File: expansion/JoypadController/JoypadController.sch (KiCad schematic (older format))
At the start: 2 parts

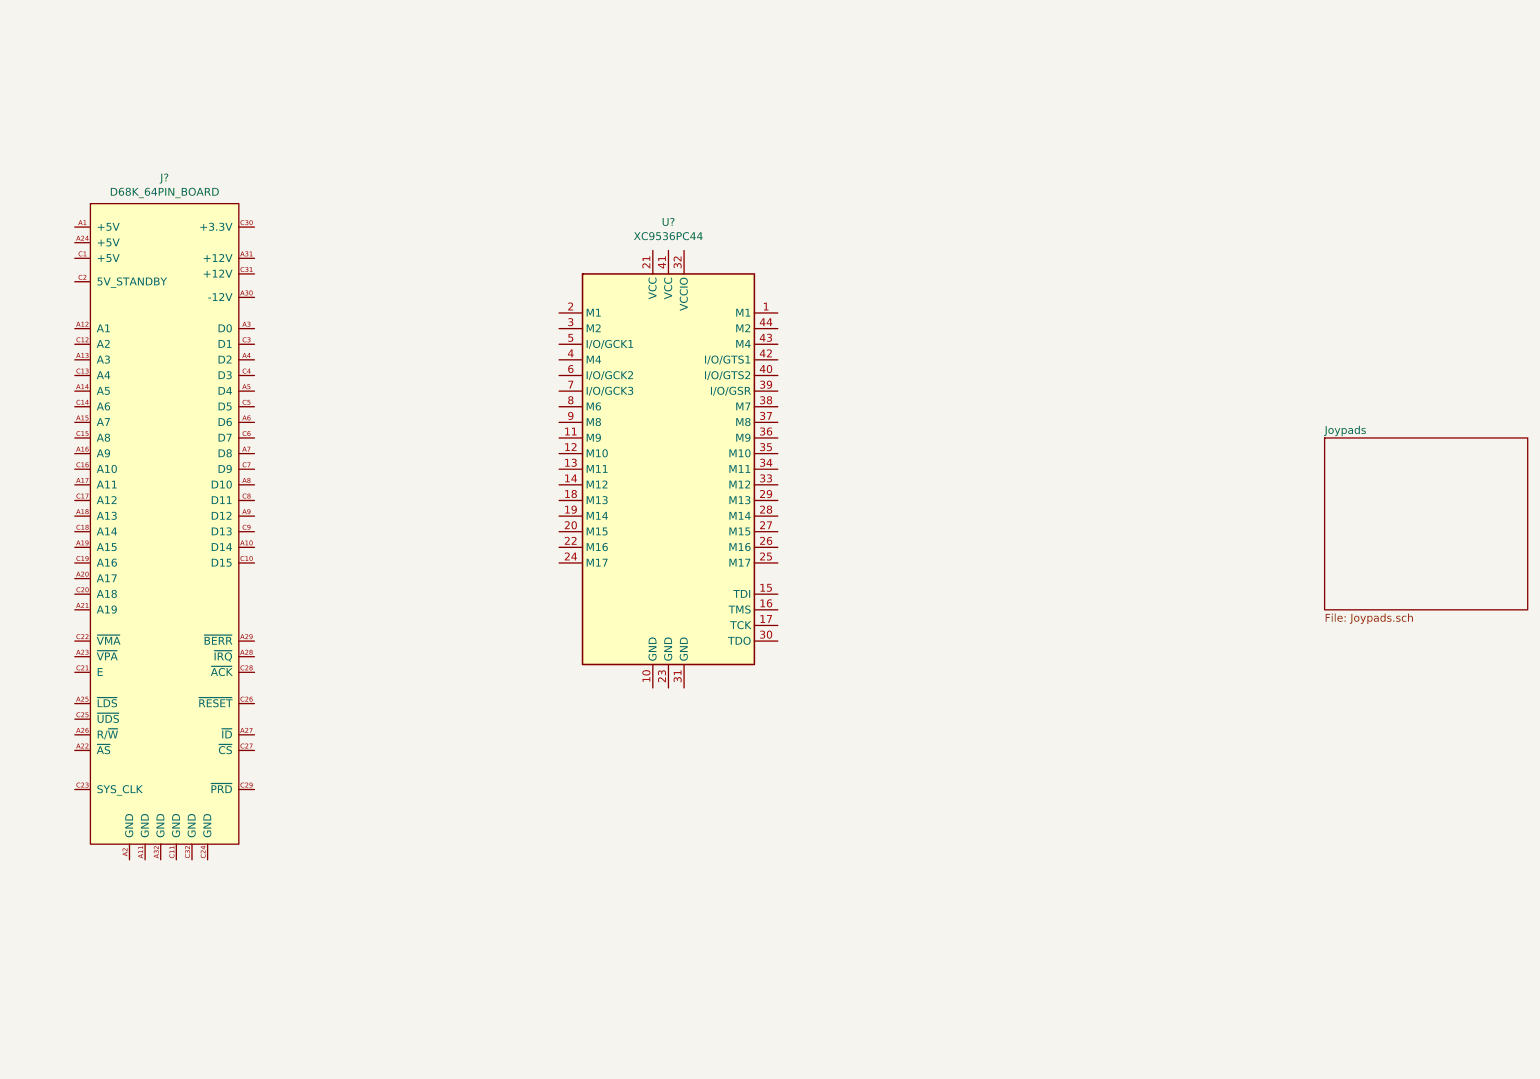
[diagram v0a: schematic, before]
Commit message: Added PCB for Joypad controller
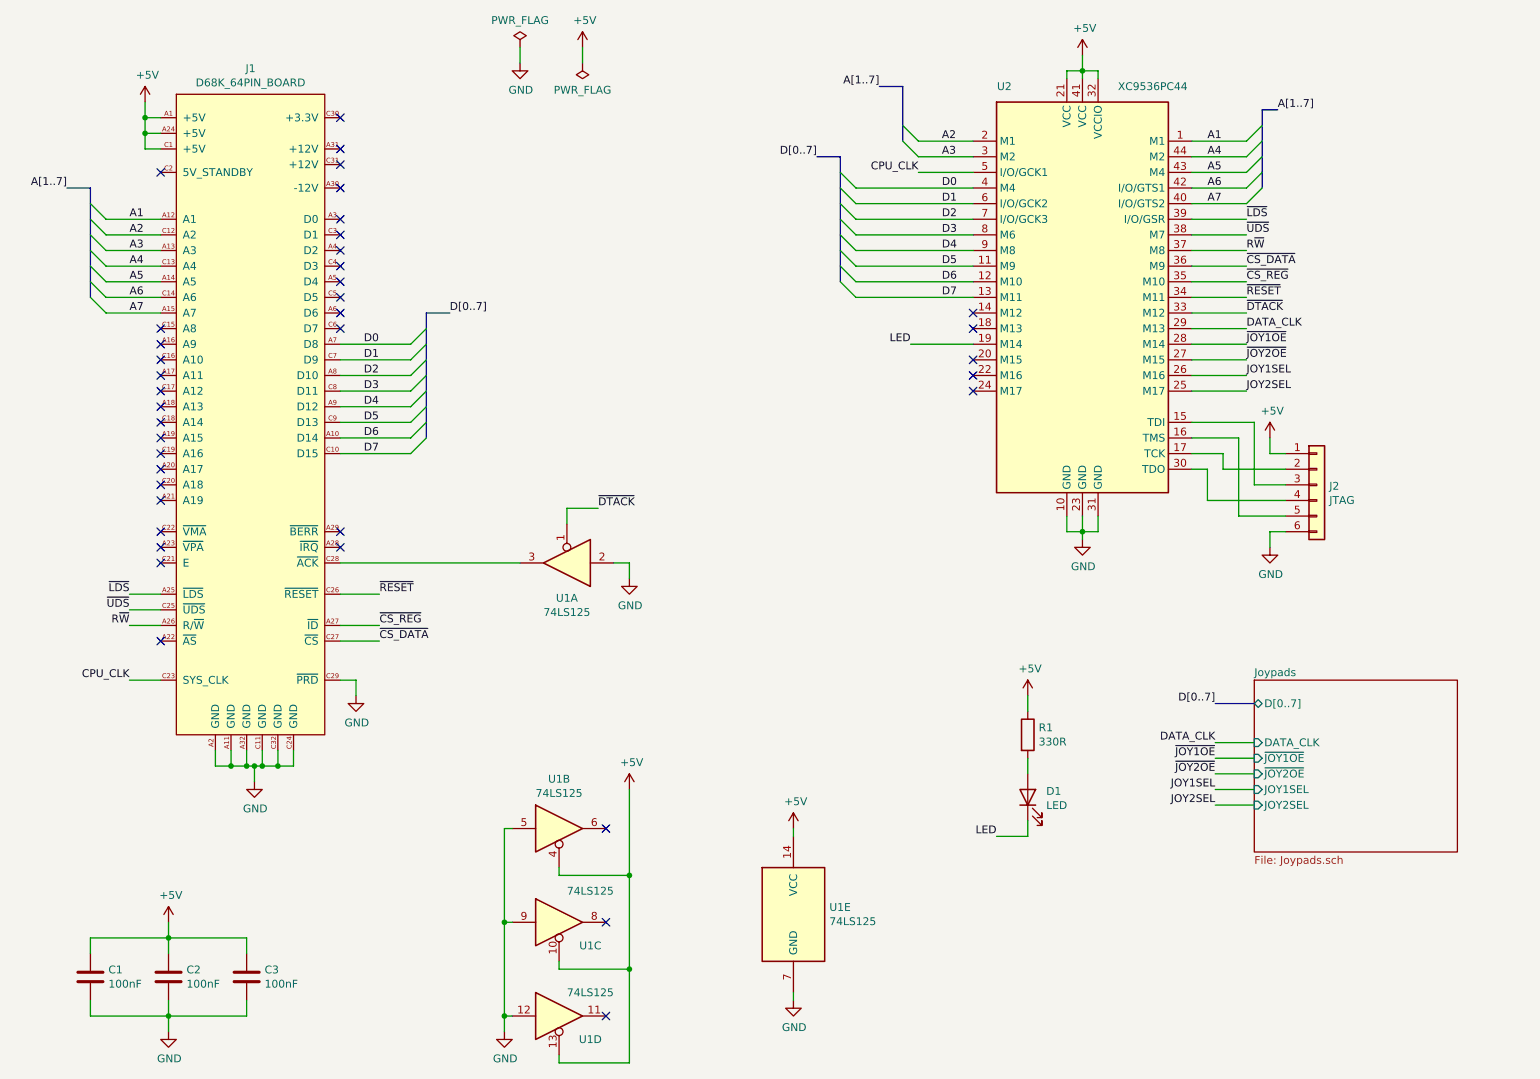
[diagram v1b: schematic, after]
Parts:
- added C1, C2, C3: 100nF, Capacitor_THT:C_Disc_D5.0mm_W2.5mm_P2.50mm, symbol Device:C
- added D1: LED, LED_THT:LED_D5.0mm, symbol Device:LED
- added J2: JTAG, Connector_PinHeader_2.54mm:PinHeader_1x06_P2.54mm_Vertical, symbol Connector_Generic:Conn_01x06
- added R1: 330R, Resistor_THT:R_Axial_DIN0207_L6.3mm_D2.5mm_P10.16mm_Horizontal, symbol Device:R
- added U1: 74LS125, Package_DIP:DIP-14_W7.62mm_Socket, symbol 74xx:74LS125
- U2: renamed from U?; footprint (none) -> Package_LCC:PLCC-44
- gave numbers to parts that had none: 1
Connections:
- net +5V: now reaches J1.A1 (+5V)
- net +5V: now also J1.A24 (+5V), J1.C1 (+5V), U2.21 (VCC), U2.32 (VCCIO), U2.41 (VCC), C1.1, C2.1, C3.1, J2.1 (Pin_1), R1.1, U1.10, U1.13, U1.14 (VCC), U1.4
- net D6: now reaches J1.A10 (D14)
- net D6: now also U2.12 (M10)
- net GND: now reaches J1.A11 (GND)
- net GND: now also J1.A2 (GND), J1.A32 (GND), J1.C11 (GND), J1.C24 (GND), J1.C29 (~PRD), J1.C32 (GND), U2.10 (GND), U2.23 (GND), U2.31 (GND), C1.2, C2.2, C3.2, J2.6 (Pin_6), U1.12, U1.2, U1.5, U1.7 (GND), U1.9
- net A1: now reaches J1.A12 (A1)
- net A1: now also U2.1 (M1)
- net A3: now reaches J1.A13 (A3)
- net A3: now also U2.3 (M2)
- net A5: now reaches J1.A14 (A5)
- net A5: now also U2.43 (M4)
- net A7: now reaches J1.A15 (A7)
- net A7: now also U2.40 (I/O/GTS2)
- net ~LDS: now reaches J1.A25 (~LDS)
- net ~LDS: now also U2.39 (I/O/GSR)
- net R~W: now reaches J1.A26 (R/~W)
- net R~W: now also U2.37 (M8)
- net ~CS_REG: now reaches J1.A27 (~ID)
- net ~CS_REG: now also U2.35 (M10)
- net D0: now reaches J1.A7 (D8)
- net D0: now also U2.4 (M4)
- net D2: now reaches J1.A8 (D10)
- net D2: now also U2.7 (I/O/GCK3)
- net D4: now reaches J1.A9 (D12)
- net D4: now also U2.9 (M8)
- net D7: now reaches J1.C10 (D15)
- net D7: now also U2.13 (M11)
- net A2: now reaches J1.C12 (A2)
- net A2: now also U2.2 (M1)
- net A4: now reaches J1.C13 (A4)
- net A4: now also U2.44 (M2)
- net A6: now reaches J1.C14 (A6)
- net A6: now also U2.42 (I/O/GTS1)
- net CPU_CLK: now reaches J1.C23 (SYS_CLK)
- net CPU_CLK: now also U2.5 (I/O/GCK1)
- net ~UDS: now reaches J1.C25 (~UDS)
- net ~UDS: now also U2.38 (M7)
- net ~RESET: now reaches J1.C26 (~RESET)
- net ~RESET: now also U2.34 (M11)
- net ~CS_DATA: now reaches J1.C27 (~CS)
- net ~CS_DATA: now also U2.36 (M9)
- net at J1.C28 (~ACK): now also U1.3
- net D1: now reaches J1.C7 (D9)
- net D1: now also U2.6 (I/O/GCK2)
- net D3: now reaches J1.C8 (D11)
- net D3: now also U2.8 (M6)
- net D5: now reaches J1.C9 (D13)
- net D5: now also U2.11 (M9)
- net at U2.15 (TDI): now also J2.3 (Pin_3)
- net at U2.16 (TMS): now also J2.5 (Pin_5)
- net at U2.17 (TCK): now also J2.2 (Pin_2)
- net LED: now reaches U2.19 (M14)
- net LED: now also D1.1 (K)
- net JOY2SEL: now reaches U2.25 (M17)
- net JOY1SEL: now reaches U2.26 (M16)
- net ~JOY2OE: now reaches U2.27 (M15)
- net ~JOY1OE: now reaches U2.28 (M14)
- net DATA_CLK: now reaches U2.29 (M13)
- net at U2.30 (TDO): now also J2.4 (Pin_4)
- net ~DTACK: now reaches U2.33 (M12)
- net ~DTACK: now also U1.1
- new net: D1.2 (A), R1.2
- no-connect marks 0 -> 39
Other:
- moved on the sheet: J1, U2
